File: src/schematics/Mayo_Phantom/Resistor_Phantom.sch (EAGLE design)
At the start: 193 parts, among them K1 AQY221R2V, K2 AQY221R2V, K3 AQY221R2V, X1 DSUBIN

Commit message: Resistor Phantom
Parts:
- removed D3: 1N4148DO35-7, diode:1N4148DO35-7
- removed X2: (no value), con-molex:KK-156-4
- added D1: 1N4148, diode:1N4148
- added J2: 22-27-2041-04, con-molex:22-27-2041-04
- D2: value 1N4148DO35-7 -> 1N4148; device diode:1N4148DO35-7 -> diode:1N4148
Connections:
- net 5V: now also J2-1.S; no longer X2-1.S
- net ARD_GND: now also D1.A, J2-3.S; no longer D3.A, X2-2.S
- net IN: now also J2-2.S; no longer X2-3.S
- net N$21: now also D1.C; no longer D2.C
- net N$39: now also D2.C; no longer D3.C
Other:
- moved on the sheet: D2
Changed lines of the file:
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@@
 <part name="Q1" library="semicon-smd-ipc" deviceset="NPN-TRANSISTOR_" device="SOT23"/>
 <part name="L1" library="inductors" deviceset="BLM15H" device="0805MAYO"/>
-<part name="X2" library="con-molex" deviceset="KK-156-4" device=""/>
 <part name="R161" library="rcl" deviceset="R-EU_" device="R0402" value="820"/>
 <part name="R162" library="rcl" deviceset="R-EU_" device="R0402" value="3k"/>
 <part name="K2" library="relay" deviceset="AQY221*2V" device="" technology="R"/>
-<part name="D2" library="diode" deviceset="1N4148" device="DO35-7"/>
 <part name="Q2" library="semicon-smd-ipc" deviceset="NPN-TRANSISTOR_" device="SOT23"/>
 <part name="L2" library="inductors" deviceset="BLM15H" device="0805MAYO"/>
@@
 <part name="R167" library="rcl" deviceset="R-EU_" device="R0402" value="3k"/>
 <part name="K3" library="relay" deviceset="AQY221*2V" device="" technology="R"/>
-<part name="D3" library="diode" deviceset="1N4148" device="DO35-7"/>
 <part name="Q3" library="semicon-smd-ipc" deviceset="NPN-TRANSISTOR_" device="SOT23"/>
 <part name="L3" library="inductors" deviceset="BLM15H" device="0805MAYO"/>
@@
 <part name="R178" library="rcl" deviceset="R-EU_" device="R0402" value="3k"/>
 <part name="D4" library="diode" deviceset="1N4148" device=""/>
+<part name="D1" library="diode" deviceset="1N4148" device=""/>
+<part name="D2" library="diode" deviceset="1N4148" device=""/>
+<part name="J2" library="con-molex" deviceset="22-?-04" device="27-2041"/>
 </parts>
 <sheets>
@@
 <instance part="Q1" gate="G$1" x="71.12" y="205.74"/>
 <instance part="L1" gate="G$1" x="96.52" y="213.36"/>
-<instance part="X2" gate="-1" x="12.7" y="241.3"/>
-<instance part="X2" gate="-2" x="12.7" y="236.22"/>
-<instance part="X2" gate="-3" x="12.7" y="231.14"/>
 <instance part="R161" gate="G$1" x="83.82" y="231.14" rot="R270"/>
 <instance part="R162" gate="G$1" x="58.42" y="205.74"/>
 <instance part="K2" gate="G$1" x="264.16" y="208.28"/>
-<instance part="D2" gate="G$1" x="231.14" y="205.74" rot="R90"/>
 <instance part="Q2" gate="G$1" x="218.44" y="205.74"/>
 <instance part="L2" gate="G$1" x="243.84" y="213.36"/>
@@
 <instance part="R167" gate="G$1" x="205.74" y="205.74"/>
 <instance part="K3" gate="G$1" x="408.94" y="210.82"/>
-<instance part="D3" gate="G$1" x="375.92" y="208.28" rot="R90"/>
 <instance part="Q3" gate="G$1" x="363.22" y="208.28"/>
 <instance part="L3" gate="G$1" x="388.62" y="215.9"/>
@@
 <instance part="R178" gate="G$1" x="416.56" y="17.78" rot="R270"/>
 <instance part="D4" gate="G$1" x="83.82" y="205.74" rot="R90"/>
+<instance part="D1" gate="G$1" x="231.14" y="205.74" rot="R90"/>
+<instance part="D2" gate="G$1" x="375.92" y="208.28" rot="R90"/>
+<instance part="J2" gate="-1" x="-10.16" y="241.3"/>
+<instance part="J2" gate="-2" x="-10.16" y="236.22"/>
+<instance part="J2" gate="-3" x="-10.16" y="231.14"/>
+<instance part="J2" gate="-4" x="-10.16" y="226.06"/>
 </instances>
 <busses>
@@
 <net name="5V" class="0">
 <segment>
-<pinref part="X2" gate="-1" pin="S"/>
-<wire x1="10.16" y1="241.3" x2="5.08" y2="241.3" width="0.1524" layer="91"/>
-<label x="5.08" y="241.3" size="1.778" layer="95" rot="R180" xref="yes"/>
-</segment>
-<segment>
 <pinref part="R161" gate="G$1" pin="1"/>
 <wire x1="83.82" y1="236.22" x2="83.82" y2="241.3" width="0.1524" layer="91"/>
@@
 <label x="375.92" y="243.84" size="1.778" layer="95" rot="R90" xref="yes"/>
 </segment>
+<segment>
+<pinref part="J2" gate="-1" pin="S"/>
+<wire x1="-12.7" y1="241.3" x2="-15.24" y2="241.3" width="0.1524" layer="91"/>
+<label x="-15.24" y="241.3" size="1.778" layer="95" rot="R180" xref="yes"/>
+</segment>
 </net>
 <net name="ARD_GND" class="0">
-<segment>
-<pinref part="X2" gate="-2" pin="S"/>
-<wire x1="10.16" y1="236.22" x2="5.08" y2="236.22" width="0.1524" layer="91"/>
-<label x="5.08" y="236.22" size="1.778" layer="95" rot="R180" xref="yes"/>
-</segment>
 <segment>
 <pinref part="Q1" gate="G$1" pin="E"/>
@@
 <wire x1="231.14" y1="198.12" x2="254" y2="198.12" width="0.1524" layer="91"/>
 <wire x1="254" y1="198.12" x2="254" y2="205.74" width="0.1524" layer="91"/>
-<pinref part="D2" gate="G$1" pin="A"/>
 <wire x1="231.14" y1="203.2" x2="231.14" y2="198.12" width="0.1524" layer="91"/>
 <junction x="231.14" y="198.12"/>
 <wire x1="231.14" y1="198.12" x2="231.14" y2="190.5" width="0.1524" layer="91"/>
 <label x="231.14" y="190.5" size="1.778" layer="95" rot="R270" xref="yes"/>
+<pinref part="D1" gate="G$1" pin="A"/>
 </segment>
 <segment>
@@
 <wire x1="375.92" y1="200.66" x2="398.78" y2="200.66" width="0.1524" layer="91"/>
 <wire x1="398.78" y1="200.66" x2="398.78" y2="208.28" width="0.1524" layer="91"/>
-<pinref part="D3" gate="G$1" pin="A"/>
 <wire x1="375.92" y1="205.74" x2="375.92" y2="200.66" width="0.1524" layer="91"/>
 <junction x="375.92" y="200.66"/>
 <wire x1="375.92" y1="200.66" x2="375.92" y2="193.04" width="0.1524" layer="91"/>
 <label x="375.92" y="193.04" size="1.778" layer="95" rot="R270" xref="yes"/>
+<pinref part="D2" gate="G$1" pin="A"/>
+</segment>
+<segment>
+<pinref part="J2" gate="-3" pin="S"/>
+<wire x1="-12.7" y1="231.14" x2="-15.24" y2="231.14" width="0.1524" layer="91"/>
+<label x="-15.24" y="231.14" size="1.778" layer="95" rot="R180" xref="yes"/>
 </segment>
 </net>
 <net name="IN" class="0">
-<segment>
-<pinref part="X2" gate="-3" pin="S"/>
-<wire x1="10.16" y1="231.14" x2="5.08" y2="231.14" width="0.1524" layer="91"/>
-<label x="5.08" y="231.14" size="1.778" layer="95" rot="R180" xref="yes"/>
-</segment>
 <segment>
 <pinref part="R162" gate="G$1" pin="1"/>
@@
 <wire x1="345.44" y1="208.28" x2="337.82" y2="208.28" width="0.1524" layer="91"/>
 <label x="337.82" y="208.28" size="1.778" layer="95" rot="R180" xref="yes"/>
+</segment>
+<segment>
+<pinref part="J2" gate="-2" pin="S"/>
+<wire x1="-12.7" y1="236.22" x2="-15.24" y2="236.22" width="0.1524" layer="91"/>
+<label x="-15.24" y="236.22" size="1.778" layer="95" rot="R180" xref="yes"/>
 </segment>
 </net>
@@
 <wire x1="231.14" y1="213.36" x2="220.98" y2="213.36" width="0.1524" layer="91"/>
 <wire x1="220.98" y1="213.36" x2="220.98" y2="210.82" width="0.1524" layer="91"/>
-<pinref part="D2" gate="G$1" pin="C"/>
 <wire x1="231.14" y1="208.28" x2="231.14" y2="213.36" width="0.1524" layer="91"/>
 <junction x="231.14" y="213.36"/>
 <pinref part="R166" gate="G$1" pin="2"/>
 <wire x1="231.14" y1="213.36" x2="231.14" y2="226.06" width="0.1524" layer="91"/>
+<pinref part="D1" gate="G$1" pin="C"/>
 </segment>
 </net>
@@
 <wire x1="375.92" y1="215.9" x2="365.76" y2="215.9" width="0.1524" layer="91"/>
 <wire x1="365.76" y1="215.9" x2="365.76" y2="213.36" width="0.1524" layer="91"/>
-<pinref part="D3" gate="G$1" pin="C"/>
 <wire x1="375.92" y1="210.82" x2="375.92" y2="215.9" width="0.1524" layer="91"/>
 <junction x="375.92" y="215.9"/>
 <pinref part="R169" gate="G$1" pin="2"/>
 <wire x1="375.92" y1="215.9" x2="375.92" y2="228.6" width="0.1524" layer="91"/>
-</segment>
-</net>
+<pinref part="D2" gate="G$1" pin="C"/>
+</segment>
+</net>

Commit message: Resistor Phantom
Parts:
- removed D1, D2, D4: 1N4148, diode:1N4148
- removed J2: 22-27-2041-04, con-molex:22-27-2041-04
- removed L1, L2, L3: BLM15H0805MAYO, inductors:BLM15H0805MAYO
- removed Q1, Q2, Q3: (no value), semicon-smd-ipc:NPN-TRANSISTOR_SOT23
- removed R161, R166, R169: 820, rcl:R-EU_R0402
- removed R162, R167, R170: 3k, rcl:R-EU_R0402
- added J1: 22-27-2041-04, con-molex:22-27-2041-04
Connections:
- removed net 5V: J2-1.S, R161.1, R166.1, R169.1
- removed net IN: J2-2.S, R162.1, R167.1, R170.1
- removed net N$11: K2.A, L2.2
- removed net N$21: D1.C, L2.1, Q2.C, R166.2
- removed net N$27: K1.A, L1.2
- removed net N$35: D4.C, L1.1, Q1.C, R161.2
- removed net N$36: Q2.B, R167.2
- removed net N$37: Q1.B, R162.2
- removed net N$38: K3.A, L3.2
- removed net N$39: D2.C, L3.1, Q3.C, R169.2
- removed net N$40: Q3.B, R170.2
- new net IN1: J1-1.S, K1.A
- new net IN2: J1-2.S, K2.A
- new net IN3: J1-3.S, K3.A
- net ARD_GND: now also J1-4.S; no longer D1.A, D2.A, D4.A, J2-3.S, Q1.E, Q2.E, Q3.E

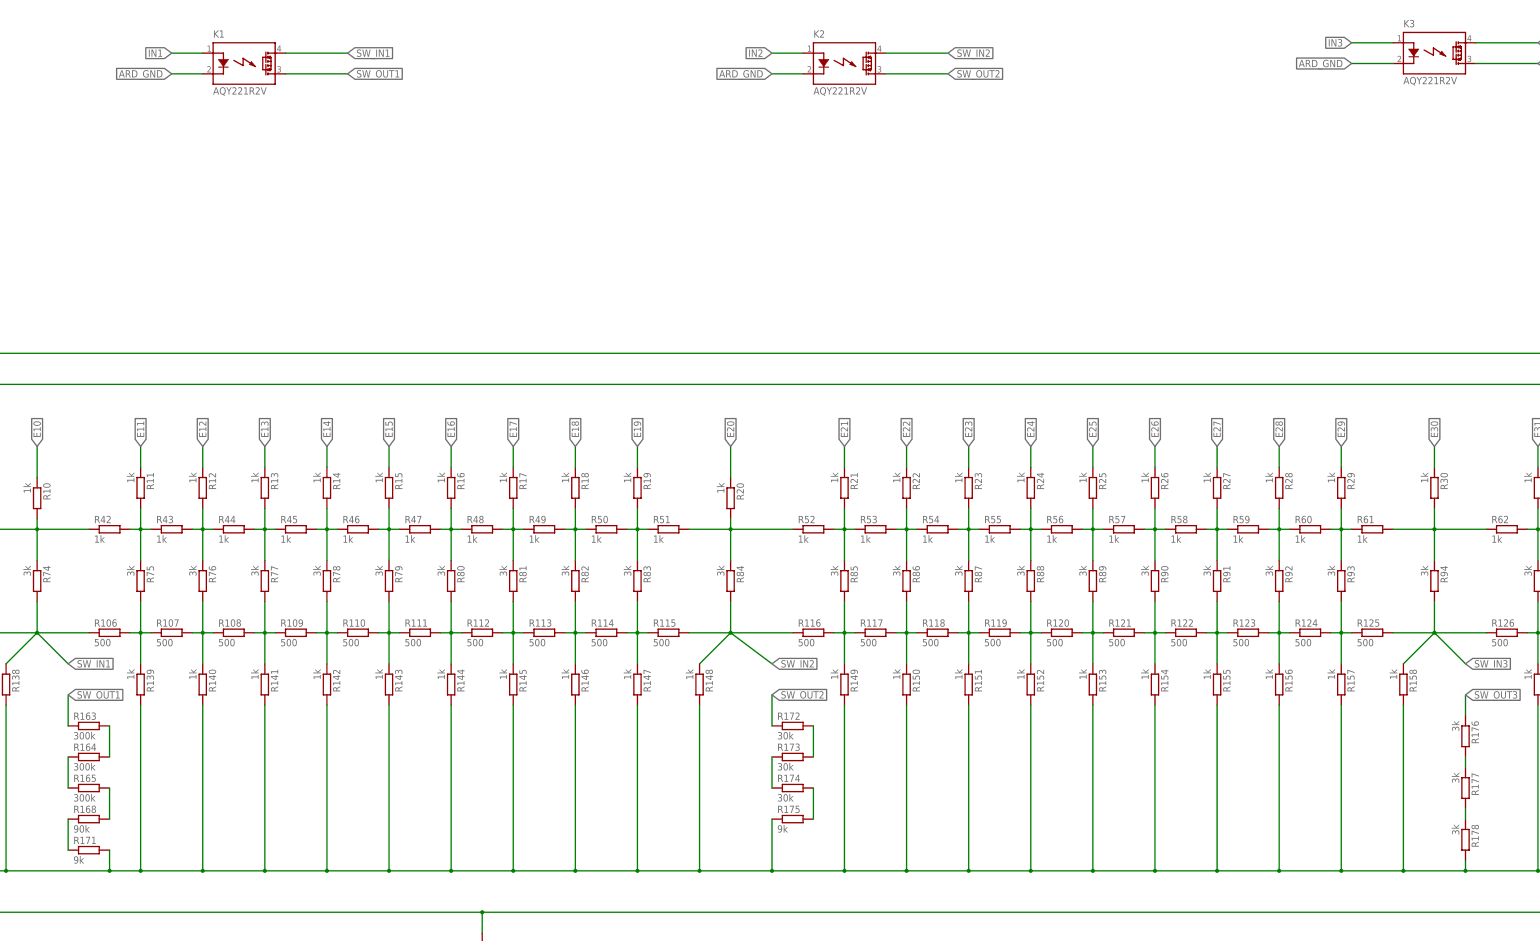
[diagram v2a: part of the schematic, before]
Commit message: Resistor Phantom v1
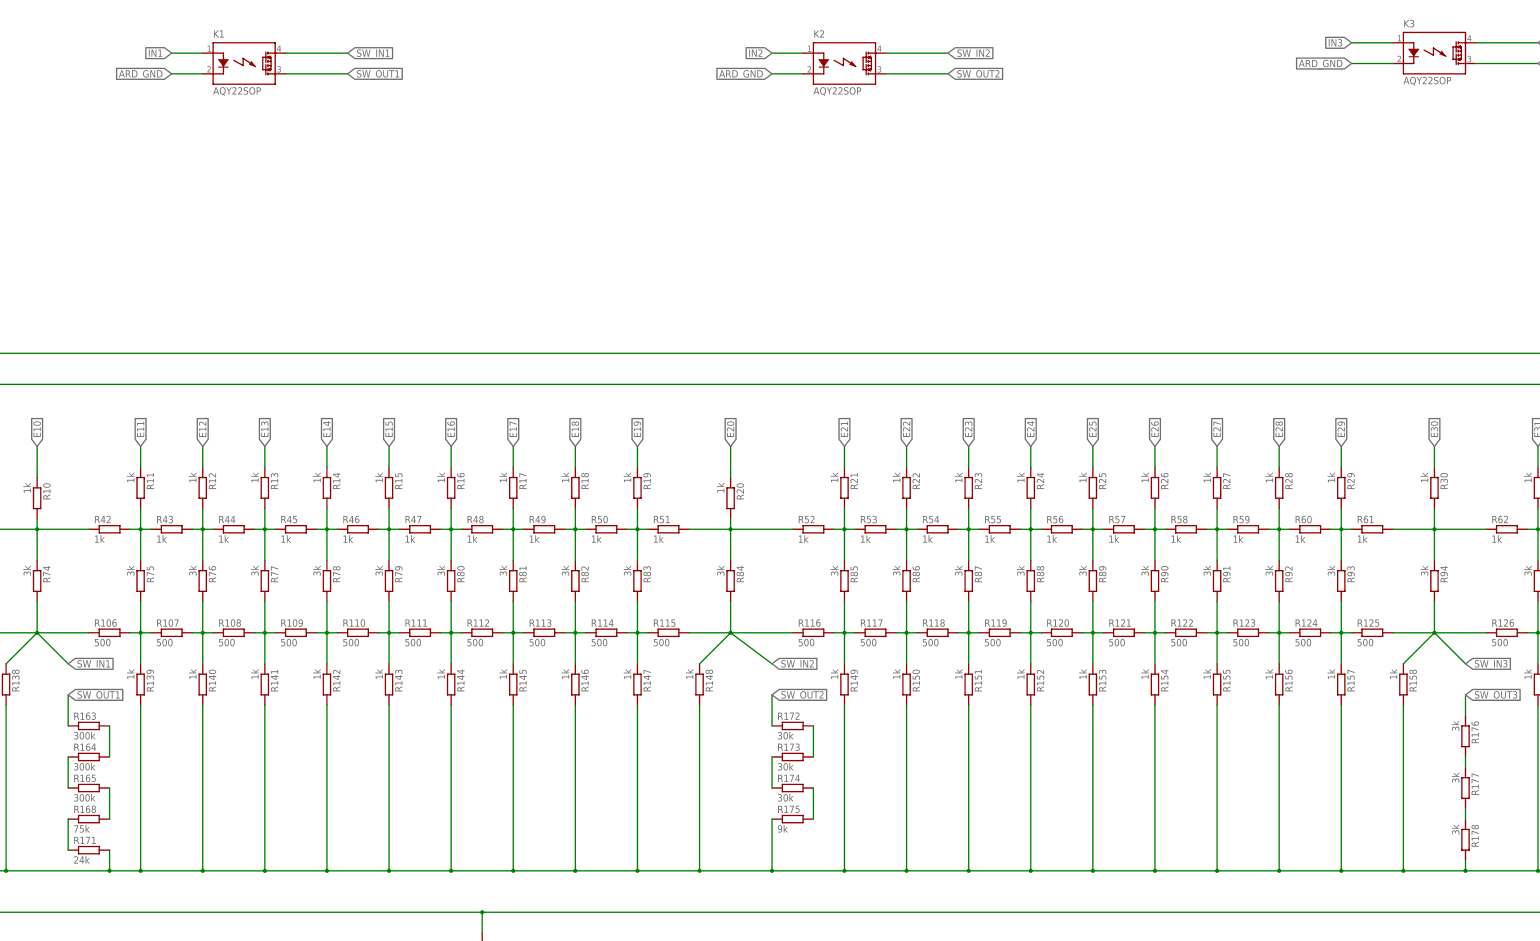
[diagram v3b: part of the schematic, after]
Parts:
- K1, K2, K3: value AQY221R2V -> AQY22SOP; device relay:AQY221R2V -> relay:AQY22SOP
- R168: value 90k -> 75k
- R171: value 9k -> 24k
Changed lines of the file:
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@@
 <part name="R159" library="rcl" deviceset="R-EU_" device="R0402" value="1k"/>
 <part name="R160" library="rcl" deviceset="R-EU_" device="R0402" value="1k"/>
-<part name="K1" library="relay" deviceset="AQY221*2V" device="" technology="R"/>
-<part name="K2" library="relay" deviceset="AQY221*2V" device="" technology="R"/>
-<part name="K3" library="relay" deviceset="AQY221*2V" device="" technology="R"/>
+<part name="K1" library="relay" deviceset="AQY*" device="SOP" technology="22" value="AQY22SOP"/>
+<part name="K2" library="relay" deviceset="AQY*" device="SOP" technology="22" value="AQY22SOP"/>
+<part name="K3" library="relay" deviceset="AQY*" device="SOP" technology="22" value="AQY22SOP"/>
 <part name="R163" library="rcl" deviceset="R-EU_" device="R0402" value="300k"/>
 <part name="R164" library="rcl" deviceset="R-EU_" device="R0402" value="300k"/>
 <part name="R165" library="rcl" deviceset="R-EU_" device="R0402" value="300k"/>
-<part name="R168" library="rcl" deviceset="R-EU_" device="R0402" value="90k"/>
-<part name="R171" library="rcl" deviceset="R-EU_" device="R0402" value="9k"/>
+<part name="R168" library="rcl" deviceset="R-EU_" device="R0402" value="75k"/>
+<part name="R171" library="rcl" deviceset="R-EU_" device="R0402" value="24k"/>
 <part name="R172" library="rcl" deviceset="R-EU_" device="R0402" value="30k"/>
 <part name="R173" library="rcl" deviceset="R-EU_" device="R0402" value="30k"/>
